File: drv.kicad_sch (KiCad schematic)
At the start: 15 parts, among them J31 Conn_01x04, U17 TMC2241ATC

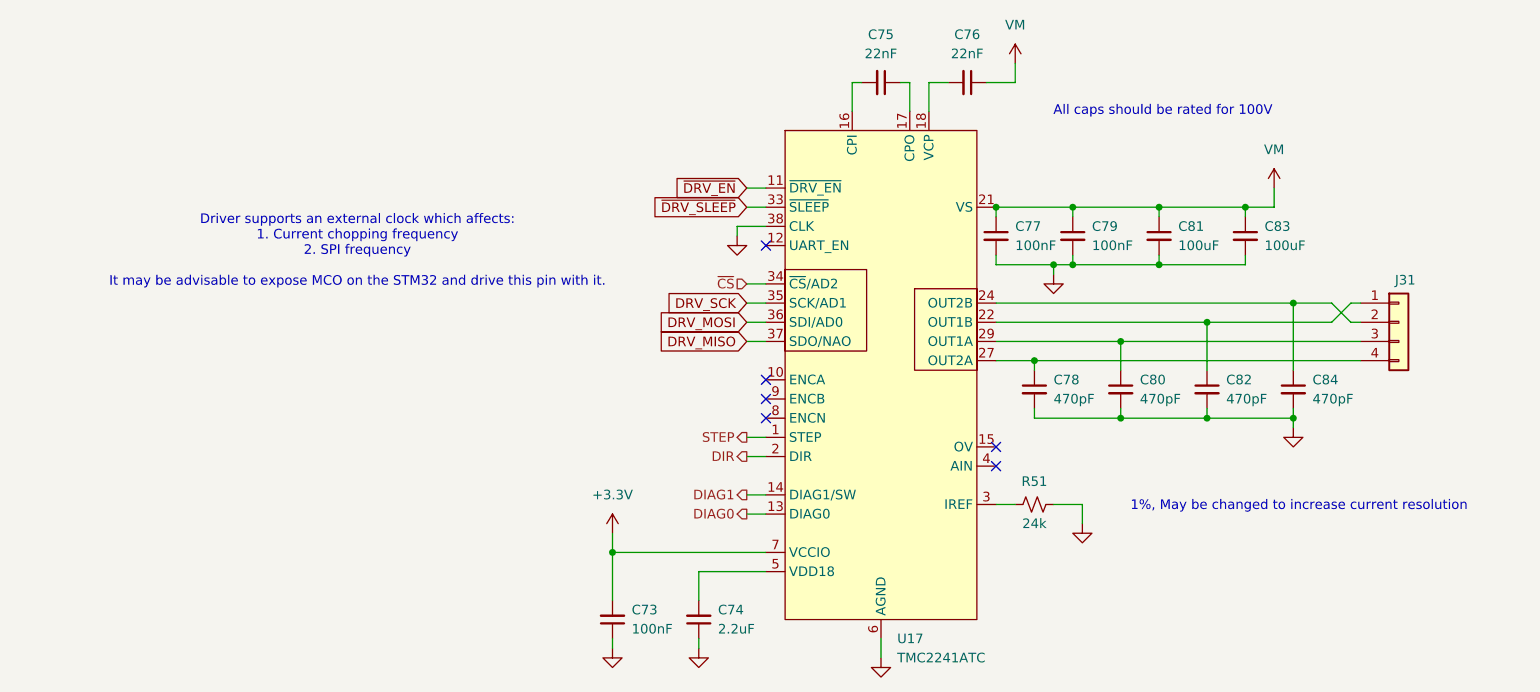
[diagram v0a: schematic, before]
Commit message: Soften scope, begin layout, reorganize sheets (still need to delete extras)
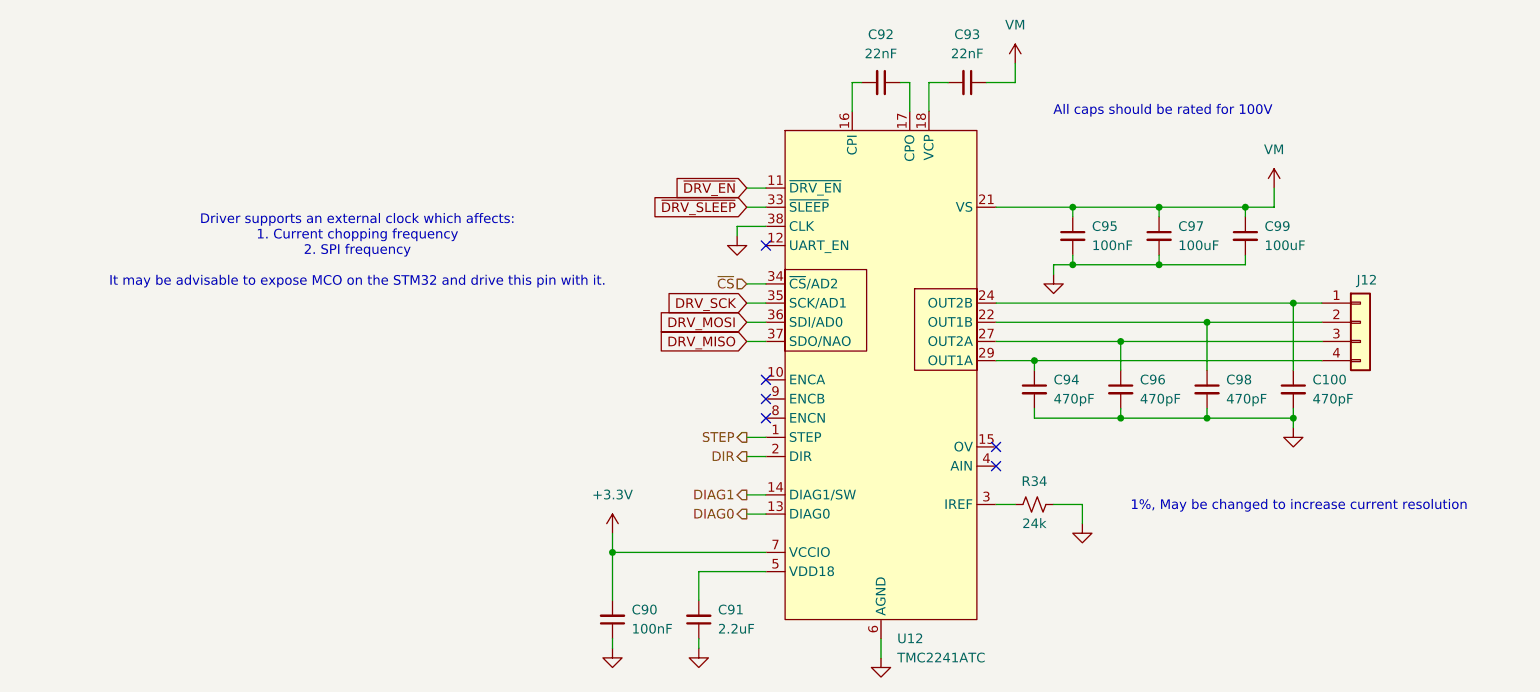
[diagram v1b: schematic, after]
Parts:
- removed C73, C77, C79: 100nF, APRLPrints:C_0603, symbol Device:C_Small
- removed C74: 2.2uF, APRLPrints:C_0603, symbol Device:C_Small
- removed C75, C76: 22nF, APRLPrints:C_0603, symbol Device:C_Small
- removed C78, C80, C82, C84: 470pF, APRLPrints:C_0603, symbol Device:C_Small
- removed C81, C83: 100uF, Capacitor_SMD:CP_Elec_10x10.5, symbol Device:C_Small
- removed J31: Conn_01x04, Connector_JST:JST_XH_B4B-XH-AM_1x04_P2.50mm_Vertical, symbol Connector_Generic:Conn_01x04
- removed R51: 24k, APRLPrints:R_0603, symbol Device:R_Small_US
- removed U17: TMC2241ATC, libserie:QFN-38_EP_5.63x7.6_Pitch0.5mm, symbol libserie:TMC2241ATC
- added C100, C94, C96, C98: 470pF, APRLPrints:C_0402, symbol Device:C_Small
- added C90: 100nF, APRLPrints:C_0402, symbol Device:C_Small
- added C91: 2.2uF, APRLPrints:C_0603, symbol Device:C_Small
- added C92, C93: 22nF, APRLPrints:C_0402, symbol Device:C_Small
- added C95: 100nF, Capacitor_SMD:CP_Elec_10x10.5, symbol Device:C_Small
- added C97, C99: 100uF, Capacitor_SMD:CP_Elec_10x10.5, symbol Device:C_Small
- added J12: Conn_01x04, Connector_JST:JST_XH_B4B-XH-AM_1x04_P2.50mm_Vertical, symbol Connector_Generic:Conn_01x04
- added R34: 24k, APRLPrints:R_0402, symbol Device:R_Small_US
- added U12: TMC2241ATC, libserie:QFN-38_EP_5.63x7.6_Pitch0.5mm, symbol libserie:TMC2241ATC
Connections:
- net +3.3V: now also C90.2, U12.7 (VCCIO)
- net DIAG0: now also U12.13 (DIAG0)
- net DIAG1: now also U12.14 (DIAG1/SW)
- net DIR: now also U12.2 (DIR)
- net DRV_MISO: now also U12.37 (SDO/NAO)
- net DRV_MOSI: now also U12.36 (SDI/AD0)
- net DRV_SCK: now also U12.35 (SCK/AD1)
- net EP: now also C100.2, C90.1, C91.1, C94.2, C95.2, C96.2, C97.2, C98.2, C99.2, R34.2, U12.23 (PGND), U12.28 (PGND), U12.38 (CLK), U12.39 (EP), U12.6 (AGND)
- net STEP: now also U12.1 (STEP)
- net VM: now also C93.1, C95.1, C97.1, C99.1, U12.21 (VS), U12.25 (VS), U12.26 (VS), U12.30 (VS)
- net ~{CS}: now also U12.34 (~{CS}/AD2)
- net ~{DRV_EN}: now also U12.11 (~{DRV_EN})
- net ~{DRV_SLEEP}: now also U12.33 (~{SLEEP})
- new net: C98.1, J12.2 (Pin_2), U12.22 (OUT1B)
- new net: C94.1, J12.4 (Pin_4), U12.29 (OUT1A)
- new net: C92.2, U12.16 (CPI)
- new net: C92.1, U12.17 (CPO)
- new net: C93.2, U12.18 (VCP)
- new net: U12.19 (NC), U12.20 (NC), U12.31 (NC), U12.32 (NC)
- new net: C100.1, J12.1 (Pin_1), U12.24 (OUT2B)
- new net: C96.1, J12.3 (Pin_3), U12.27 (OUT2A)
- new net: R34.1, U12.3 (IREF)
- new net: C91.2, U12.5 (VDD18)
